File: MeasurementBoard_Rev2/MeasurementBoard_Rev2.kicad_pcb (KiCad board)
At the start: 4 copper layers, 70 x 71.2 mm, 117 parts, among them CN1 Conn_02x19_Odd_Even, CN2 Conn_02x19_Odd_Even, CN3 522070860, CN4 Conn_01x02_Pin, CN5 Conn_01x02_Pin, CN6 Conn_01x02_Pin, CN7 Conn_01x02_Pin, J1 MIllMaxSpringConnector, J2 MIllMaxSpringConnector, J3 MIllMaxSpringConnector, J4 MIllMaxSpringConnector, J5 MIllMaxSpringConnector, J6 MIllMaxSpringConnector, J7 MIllMaxSpringConnector, J8 MIllMaxSpringConnector, U10 LTC6252, U11 ADA4807-1, U12 LTC6252, U13 ADA4807-1, U14 LTC6252, U15 ADA4807-1, U16 LTC6252, U17 ADA4807-1, U2 ADA4807-2ACP, U3 ADR4530, U4 ADA4807-2ACP, U5 ADP7118-1.8, U6 ADA4807-2ACP, U7 AD4002_LFSCP-10, U8 AD4002_LFSCP-10, U9 LD39200_Fixed

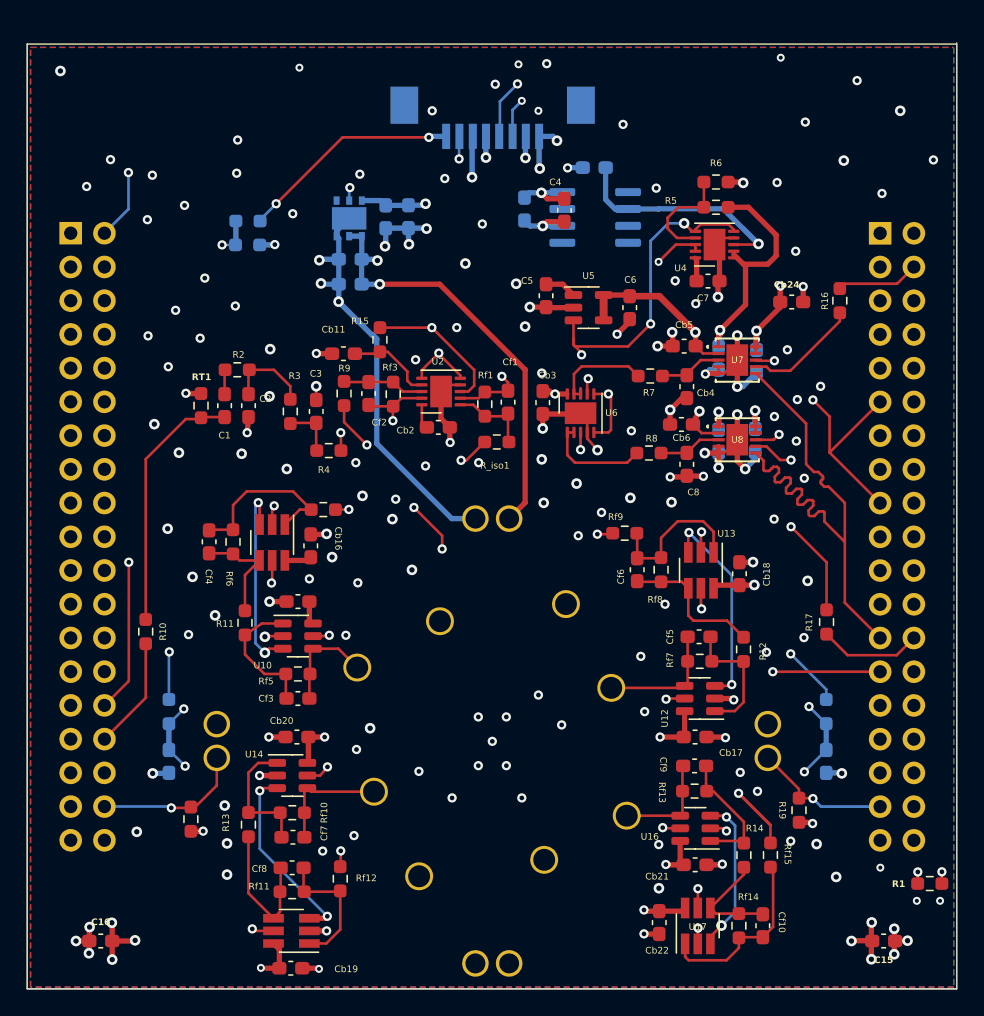
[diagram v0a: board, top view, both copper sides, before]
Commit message: Finished Measurement Board Fixes Schematic and PCB
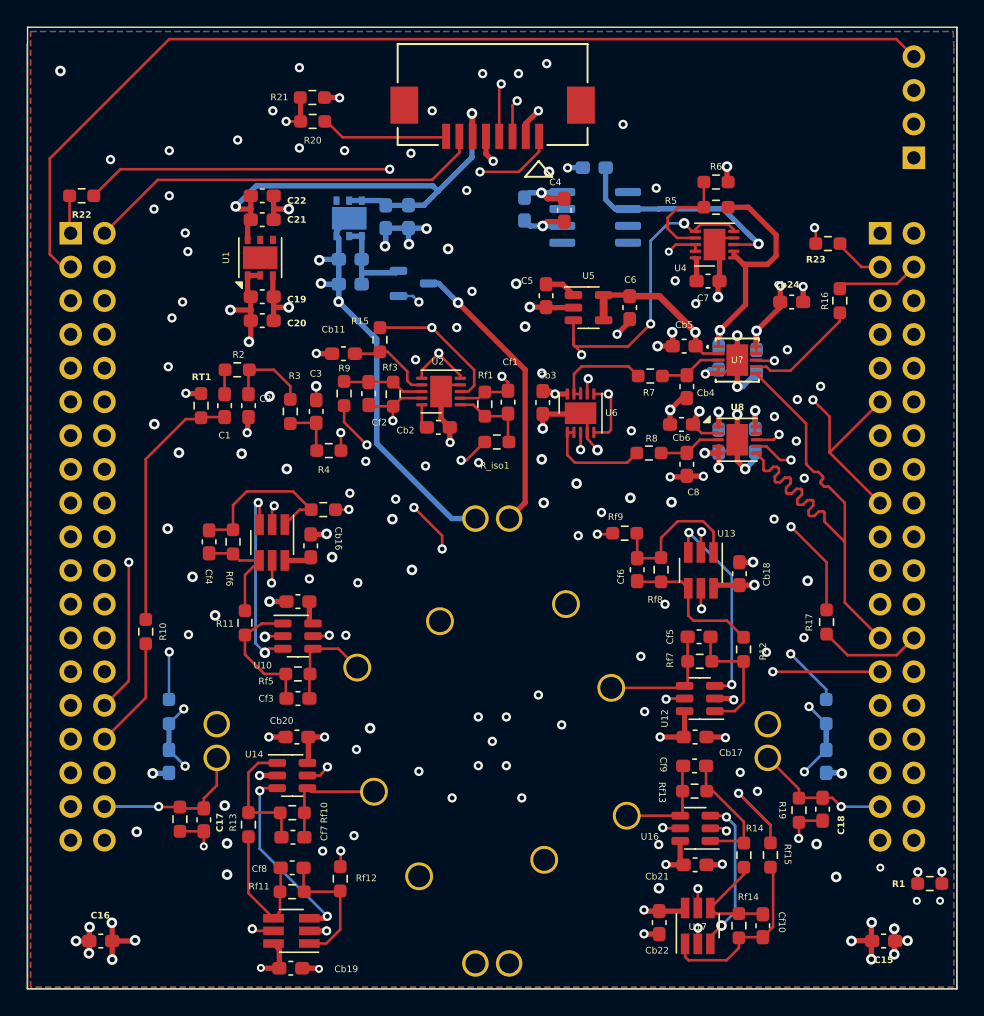
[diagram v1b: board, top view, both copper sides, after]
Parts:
- added C17: 10uF, Capacitor_SMD:C_0603_1608Metric_Pad1.08x0.95mm_HandSolder, F.Cu at (41.3, 149.4)
- added C18: 10uF, Capacitor_SMD:C_0603_1608Metric_Pad1.08x0.95mm_HandSolder, F.Cu at (87.9, 148.6)
- added C19: 100n, Capacitor_SMD:C_0603_1608Metric_Pad1.08x0.95mm_HandSolder, F.Cu at (45.7, 110.0)
- added C20: 1uF/XR5, Capacitor_SMD:C_0603_1608Metric_Pad1.08x0.95mm_HandSolder, F.Cu at (45.7, 111.8)
- added C21: 1uF/XR5, Capacitor_SMD:C_0603_1608Metric_Pad1.08x0.95mm_HandSolder, F.Cu at (45.7, 102.4)
- added C22: 100n, Capacitor_SMD:C_0603_1608Metric_Pad1.08x0.95mm_HandSolder, F.Cu at (45.7, 104.2)
- added J9: Connector to Power Switch, Connector_PinHeader_2.54mm:PinHeader_1x04_P2.54mm_Vertical, B.Cu at (94.8, 99.6)
- added Q1: SSM3J358R, Package_TO_SOT_SMD:SOT-23-3, B.Cu at (57.1, 109.0)
- added R22: 33, Resistor_SMD:R_0603_1608Metric_Pad0.98x0.95mm_HandSolder, F.Cu at (32.1, 102.4)
- added R23: 27k, Resistor_SMD:R_0603_1608Metric_Pad0.98x0.95mm_HandSolder, F.Cu at (88.3, 106.0)
- added U1: LD39200_Fixed, Package_DFN_QFN:DFN-6-1EP_3x3mm_P0.95mm_EP1.7x2.6mm, F.Cu at (45.5, 107.1)
- CN3, R20, R21: moved to F.Cu
- U8: footprint footprints:CP_10_9_ADI -> Package_CSP:LFCSP-WD-10-1EP_3x3mm_P0.5mm_EP1.64x2.38mm
- moved R21 12.1 mm to (49.5, 95.0)
- moved R20 8.95 mm to (49.5, 96.8)
- moved R18 0.82 mm to (39.5, 149.4)
- turned CN3 to 180 degrees
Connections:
- C12 pad 1: /Heater_Interface/Heater+ -> Net-(Q1-S)
- C14 pad 1: /Heater_Interface/Heater+ -> Net-(Q1-S)
- CN1 pad 1: Heater_EN -> /MCU Connections/PB11
- CN1 pad 3: unconnected-(CN1-Pin_3-Pad3) -> ~{Power_Switch_INT}
- CN2 pad 3: unconnected-(CN2-Pin_3-Pad3) -> /MCU Connections/PB8
- CN3 pad 1: V_Batt -> ~{PWR_EN}
- CN3 pad 2: ~{CHARGE_EN} -> GND
- CN3 pad 3: Vcc -> UART_RX
- CN3 pad 4: GND -> UART_TX
- CN3 pad 5: UART_TX -> GND
- CN3 pad 6: UART_RX -> Vcc
- CN3 pad 7: GND -> ~{CHARGE_EN}
- CN3 pad 8: Vdd_Main -> V_Batt
- U9 pad 1: /Heater_Interface/Heater+ -> Net-(Q1-S)
- U9 pad 2: /Heater_Interface/Heater+ -> Net-(Q1-S)
- U9 pad 5: Heater_EN -> unconnected-(U9-EN-Pad5)
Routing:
- net ~{Power_Switch_INT}: track 0.00 -> 78.5 mm
- net ~{PWR_EN}: track 0.00 -> 36.2 mm, vias 0 -> 2
- net Heater_PWM: track 0.00 -> 35.1 mm, vias 0 -> 2
- net Vcc: track 12.1 -> 36.6 mm
- net Heater_EN: track 23.4 -> 0.00 mm, vias 1 -> 0
- net GND: track 139.6 -> 153.0 mm, vias 117 -> 115
- net /MCU Connections/PC1: track 41.2 -> 52.5 mm
- net /Heater_Interface/Heater+: track 32.5 -> 21.7 mm, vias 2 -> 1
- net Net-(Q1-S): track 0.00 -> 7.41 mm
- net V_Batt: track 16.7 -> 9.65 mm, vias 2 -> 0
- net /MCU Connections/PB8: track 0.00 -> 3.86 mm
- net Vdd_Main: track 67.8 -> 71.4 mm, vias 75 -> 67
- net /MCU Connections/PB11: track 0.00 -> 2.86 mm
- net ~{CHARGE_EN}: track 32.4 -> 30.5 mm, vias 2 -> 0
- net V_MID: track 118.4 -> 119.6 mm
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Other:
- board size 70 x 71.2 mm -> 70 x 72.4 mm

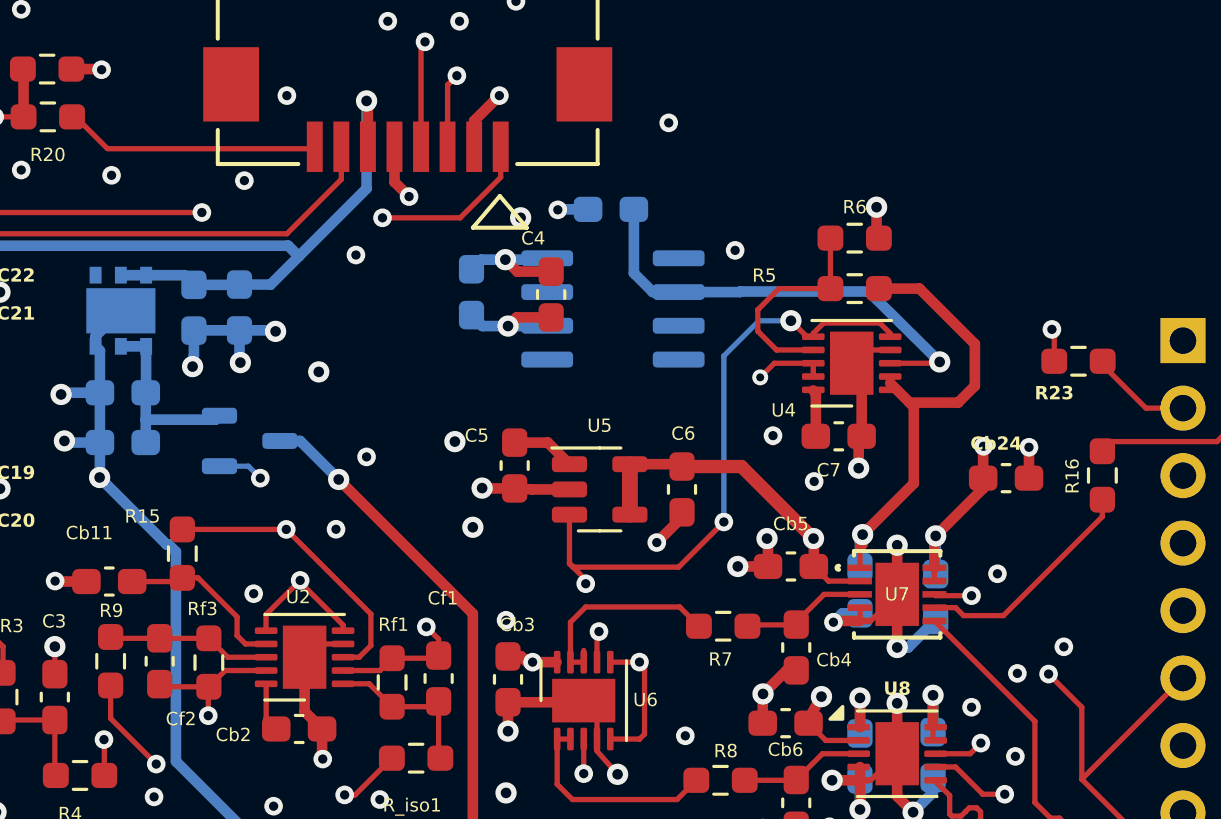
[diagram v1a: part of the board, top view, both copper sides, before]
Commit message: Updated Measurement Board with new 3V Reference
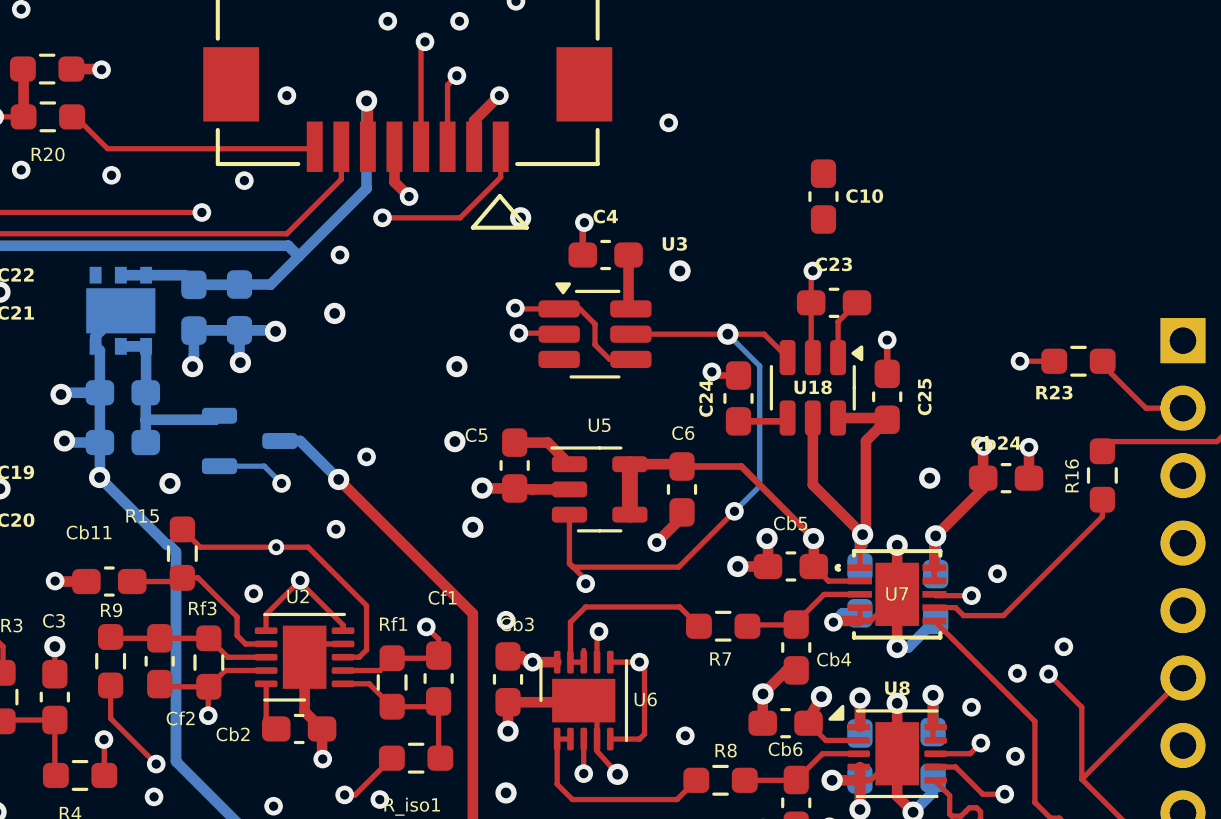
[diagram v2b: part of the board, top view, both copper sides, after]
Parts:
- removed C11, C7: 1uF, Capacitor_SMD:C_0603_1608Metric_Pad1.08x0.95mm_HandSolder
- removed R5, R6: 10k, Resistor_SMD:R_0603_1608Metric_Pad0.98x0.95mm_HandSolder
- removed U4: ADA4807-2ACP, Package_CSP:LFCSP-WD-10-1EP_3x3mm_P0.5mm_EP1.64x2.38mm
- added C23: 0.1uF, Capacitor_SMD:C_0603_1608Metric_Pad1.08x0.95mm_HandSolder, F.Cu at (79.1, 103.8)
- added C24: 0.1uF, Capacitor_SMD:C_0603_1608Metric_Pad1.08x0.95mm_HandSolder, F.Cu at (75.5, 107.4)
- added C25: 1uF, Capacitor_SMD:C_0603_1608Metric_Pad1.08x0.95mm_HandSolder, F.Cu at (81.1, 107.4)
- added U18: MAX6070BAUT30+T, Package_TO_SOT_SMD:SOT-23-6, F.Cu at (78.3, 107.0)
- C10: moved to F.Cu
- C4: value 1uF -> 0.1uF
- U3: value ADR4530 -> ADA4807-1; footprint Package_SO:SOIC-8_3.9x4.9mm_P1.27mm -> Package_TO_SOT_SMD:SOT-23-6_Handsoldering; moved to F.Cu
- moved C10 13.7 mm to (78.7, 99.8)
- moved C4 2.53 mm to (70.5, 102.0), turned to 0 degrees
- moved U3 1.17 mm to (70.1, 105.0)
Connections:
- C4 pad 1: Vdd_Main -> GND
- C4 pad 2: GND -> Vdd_Main
- U3 pad 1: unconnected-(U3-NC-Pad1) -> V_MID
- U3 pad 2: Vdd_Main -> GND
- U3 pad 3: unconnected-(U3-NC-Pad3) -> Net-(U3-+)
- U3 pad 4: GND -> V_MID
- U3 pad 5: unconnected-(U3-NC-Pad5) -> ~{ADC1_SHDN}
- U3 pad 6: Net-(U3-OUT) -> Vdd_Main
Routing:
- net Net-(U3-OUT): track 17.2 -> 0.00 mm, vias 1 -> 0
- net Net-(U4B-+): track 8.16 -> 0.00 mm
- net GND: track 153.0 -> 148.3 mm
- net ADC_VREF: track 27.3 -> 23.2 mm
- net ~{ADC1_SHDN}: track 64.5 -> 67.5 mm
- net V_MID: track 119.6 -> 116.8 mm
- net Vdd_Main: track 71.4 -> 68.7 mm, vias 67 -> 68
- net Net-(U18-FILTER): track 0.00 -> 2.36 mm
- net Heater_PWM: track 35.1 -> 33.6 mm

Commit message: Final Edit Before Check and Combine
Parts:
- added F1: 250mA Fast-Blow, Fuse:Fuse_0603_1608Metric_Pad1.05x0.95mm_HandSolder, F.Cu at (42.9, 111.0)
- added R5: 10k, Resistor_SMD:R_0603_1608Metric_Pad0.98x0.95mm_HandSolder, F.Cu at (68.5, 107.8)
- added R6: 10k, Resistor_SMD:R_0603_1608Metric_Pad0.98x0.95mm_HandSolder, F.Cu at (63.7, 106.0)
- moved J9 9.75 mm to (87.5, 93.1), turned to -90 degrees
- moved C10 2.83 mm to (75.9, 100.2), turned to 180 degrees
- moved U3 1.60 mm to (68.5, 105.0)
- moved C4 1.60 mm to (68.9, 102.0)
- moved C5 0.89 mm to (66.9, 110.8)
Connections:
- C19 pad 1: Vdd_Main -> Net-(U1-ADJ/SENSE)
- C20 pad 1: Vdd_Main -> Net-(U1-ADJ/SENSE)
- U1 pad 1: Vdd_Main -> Net-(U1-ADJ/SENSE)
- U1 pad 2: Vdd_Main -> Net-(U1-ADJ/SENSE)
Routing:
- net ADC_VREF: track 23.2 -> 36.0 mm, vias 2 -> 3
- net Net-(U1-ADJ/SENSE): track 0.00 -> 6.44 mm
- net GND: track 148.3 -> 153.3 mm, vias 115 -> 119
- net Net-(U3-+): track 0.00 -> 4.82 mm
- net Vdd_Main: track 68.7 -> 64.9 mm, vias 68 -> 70
- net ~{ADC1_SHDN}: track 67.5 -> 69.2 mm, vias 5 -> 6
- net V_MID: track 116.8 -> 115.5 mm
- net ~{Power_Switch_INT}: track 78.5 -> 79.4 mm

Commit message: Final Rev3 Commit Post Submission
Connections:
- U1 pad 5: unconnected-(U1-EN-Pad5) -> Vcc
- U1 pad 7: (no net) -> GND
- U9 pad 5: unconnected-(U9-EN-Pad5) -> Vcc
- U9 pad 7: (no net) -> GND
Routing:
- net /ABBCore_Alt/V_Drive: vias 5 -> 4
